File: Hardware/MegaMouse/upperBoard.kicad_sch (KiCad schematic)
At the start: 23 parts, among them J601 USBC, J602 PROG, U601 FT232RL

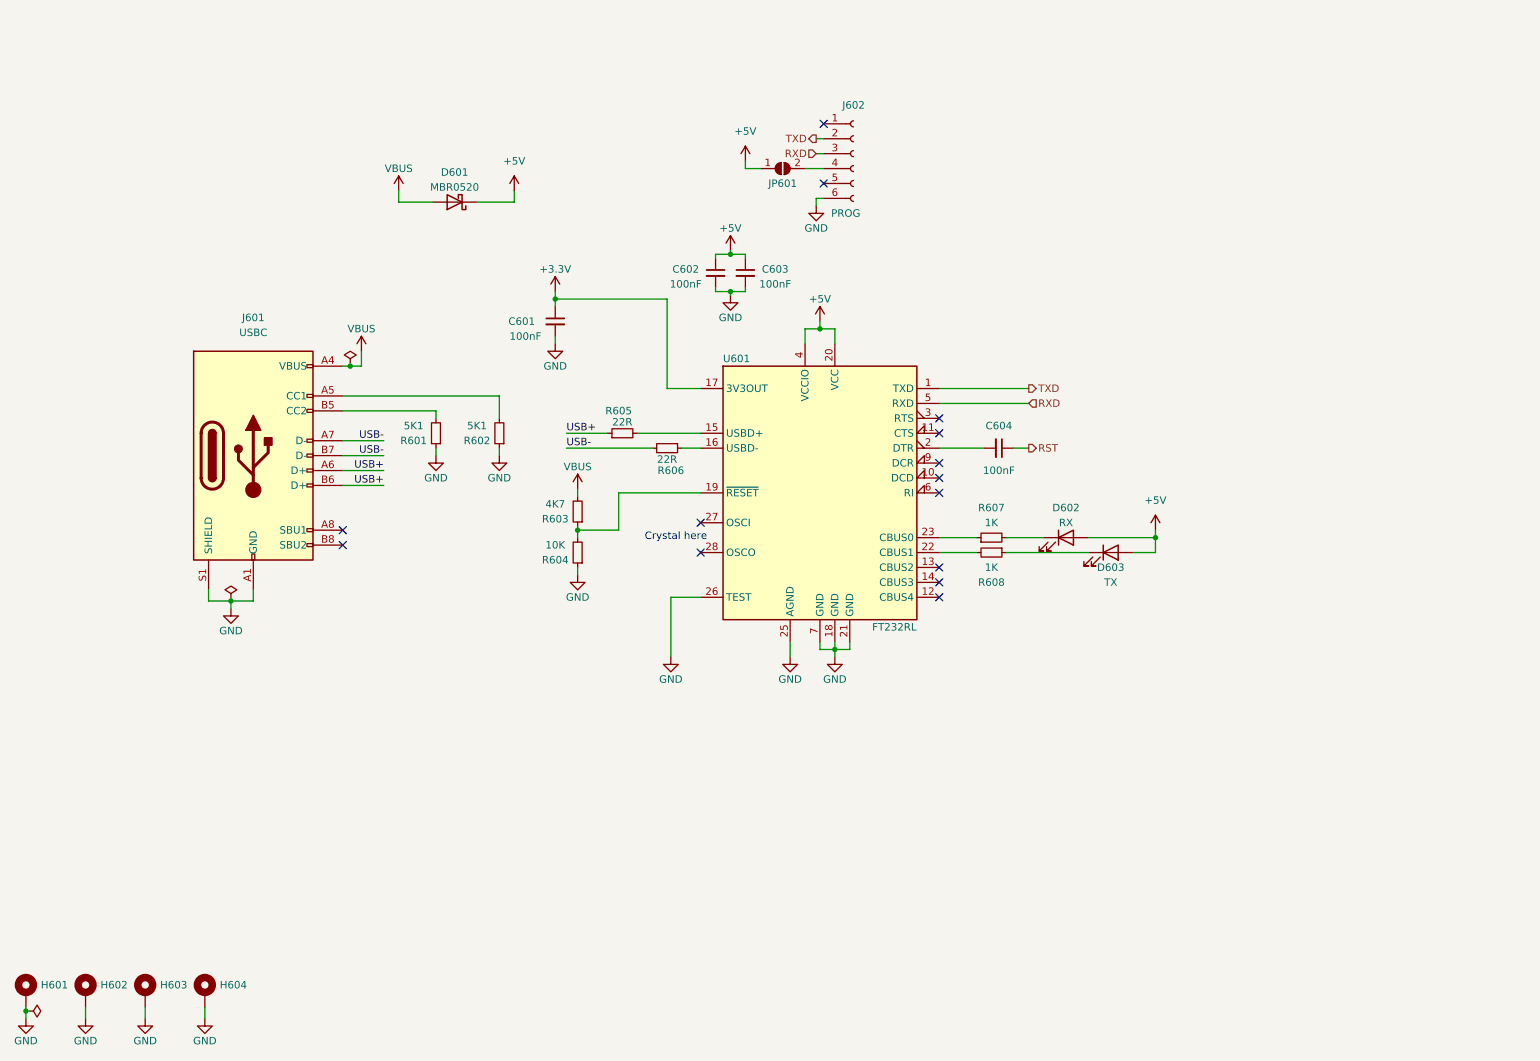
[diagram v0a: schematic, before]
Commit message: move upper body
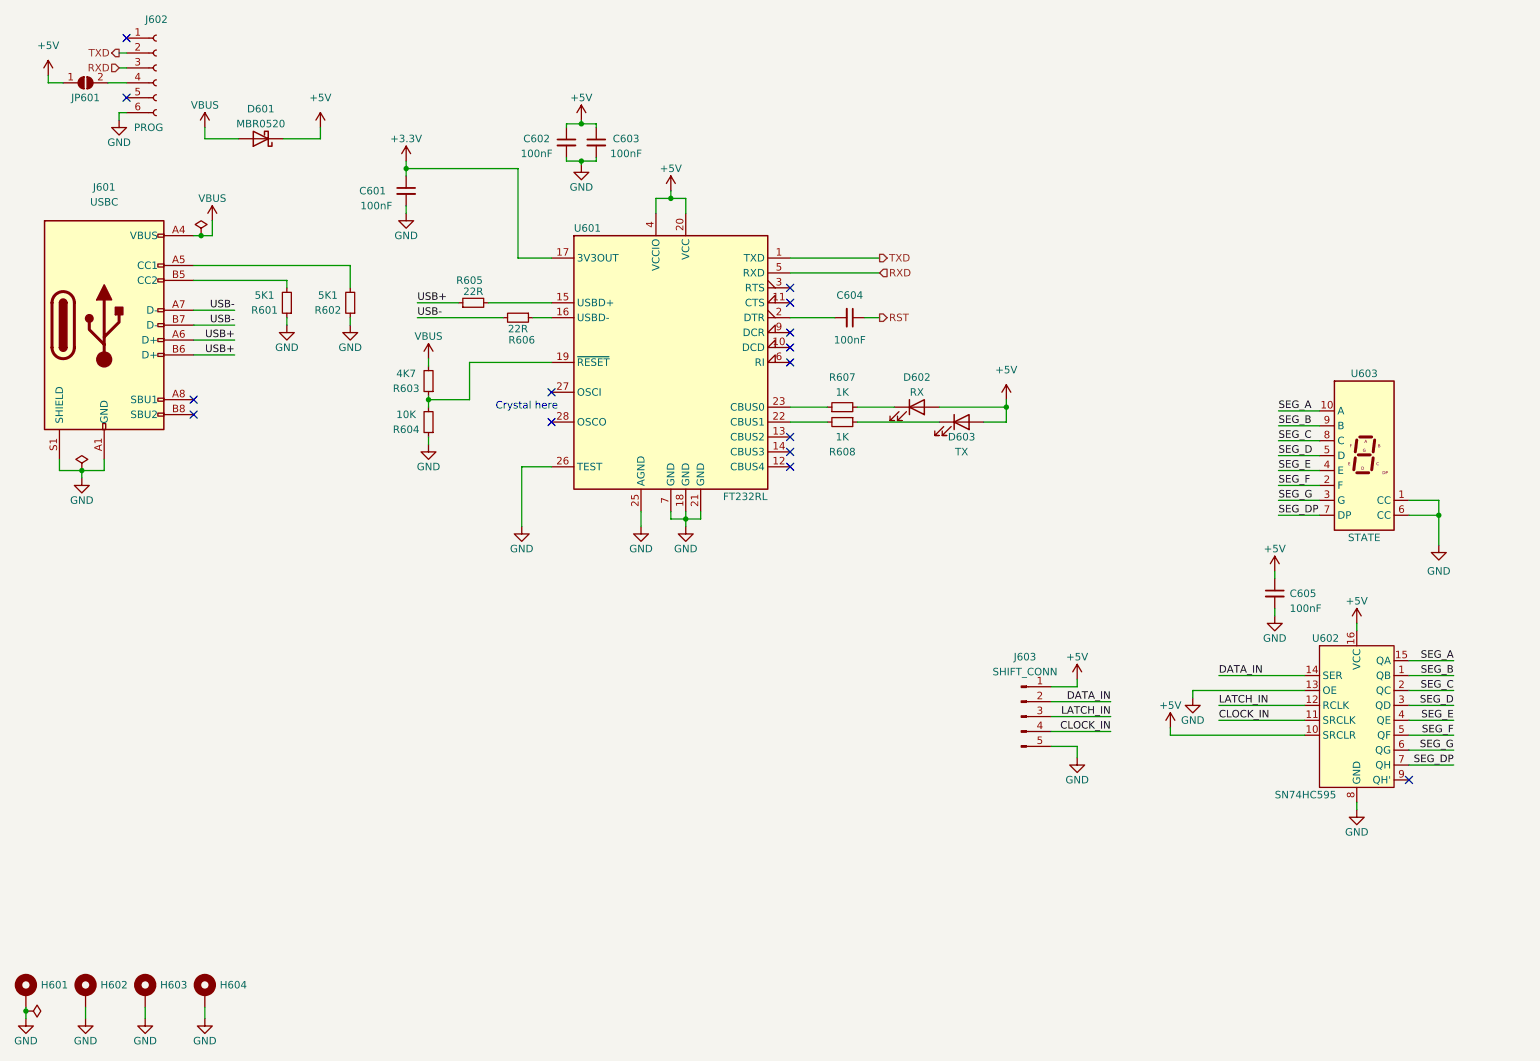
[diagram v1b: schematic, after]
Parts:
- added C605: 100nF, Capacitor_SMD:C_0805_2012Metric, symbol Device:C_Small
- added J603: SHIFT_CONN, Connector_PinHeader_2.54mm:PinHeader_1x05_P2.54mm_Vertical, symbol Connector:Conn_01x05_Male
- added U602: SN74HC595, KenwoodFox:SN74HC595, symbol KenwoodFox:SN74HC595
- added U603: STATE, Display_7Segment:HDSP-7801, symbol Display_Character:HDSP-7803
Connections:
- net +5V: now also C605.1, J603.1 (Pin_1), U602.10 (SRCLR), U602.16 (VCC)
- net GND: now also C605.2, J603.5 (Pin_5), U602.13 (OE), U602.8 (GND), U603.1 (CC), U603.6 (CC)
- new net CLOCK_IN: J603.4 (Pin_4), U602.11 (SRCLK)
- new net DATA_IN: J603.2 (Pin_2), U602.14 (SER)
- new net LATCH_IN: J603.3 (Pin_3), U602.12 (RCLK)
- new net SEG_A: U602.15 (QA), U603.10 (A)
- new net SEG_B: U602.1 (QB), U603.9 (B)
- new net SEG_C: U602.2 (QC), U603.8 (C)
- new net SEG_D: U602.3 (QD), U603.5 (D)
- new net SEG_DP: U602.7 (QH), U603.7 (DP)
- new net SEG_E: U602.4 (QE), U603.4 (E)
- new net SEG_F: U602.5 (QF), U603.2 (F)
- new net SEG_G: U602.6 (QG), U603.3 (G)
- no-connect marks 14 -> 15
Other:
- moved on the sheet: C601, C602, C603, C604, D601, D602, D603, J601, J602, JP601, R601, R602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

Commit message: Throw on second layer and target a v1.0
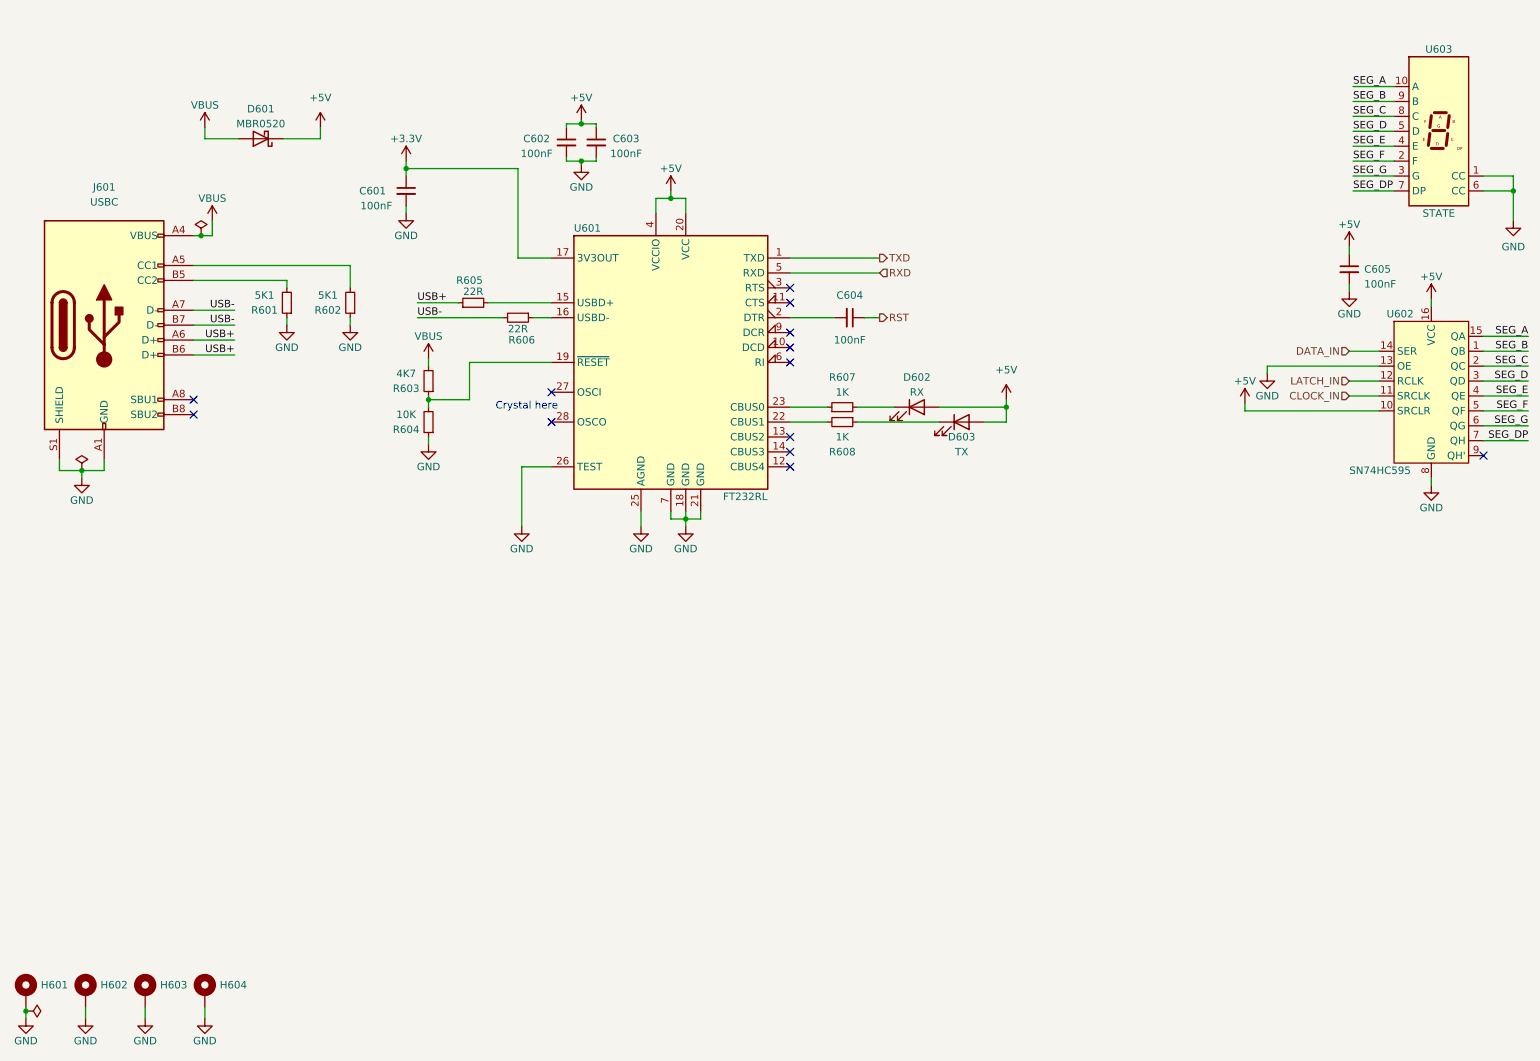
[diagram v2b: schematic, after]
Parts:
- removed J602: PROG, Connector_PinSocket_2.54mm:PinSocket_1x06_P2.54mm_Vertical, symbol Connector:Conn_01x06_Female
- removed J603: SHIFT_CONN, Connector_PinHeader_2.54mm:PinHeader_1x05_P2.54mm_Vertical, symbol Connector:Conn_01x05_Male
- removed JP601: SolderJumper_2_Open, Jumper:SolderJumper-2_P1.3mm_Open_TrianglePad1.0x1.5mm, symbol Jumper:SolderJumper_2_Open
- J601: footprint Connector_USB:USB_C_Receptacle_GCT_USB4115-03-C -> Connector_USB:USB_C_Receptacle_XKB_U262-16XN-4BVC11
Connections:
- no-connect marks 15 -> 13
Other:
- moved on the sheet: C605, U602, U603
